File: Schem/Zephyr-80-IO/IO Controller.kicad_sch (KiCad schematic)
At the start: 37 parts, among them IC1 Z80CTC, IC2 Z80SIO, IC3 Z80SIO, J5 Conn_01x08_Pin, SW1 SW_Push, SW2 SW_Push, U1 74AHCT125, U15 PIC18F57Q84-I/PT, U2 74AHCT1G125, U4 74AHC595, U5 74AHC595, U6 74HC138

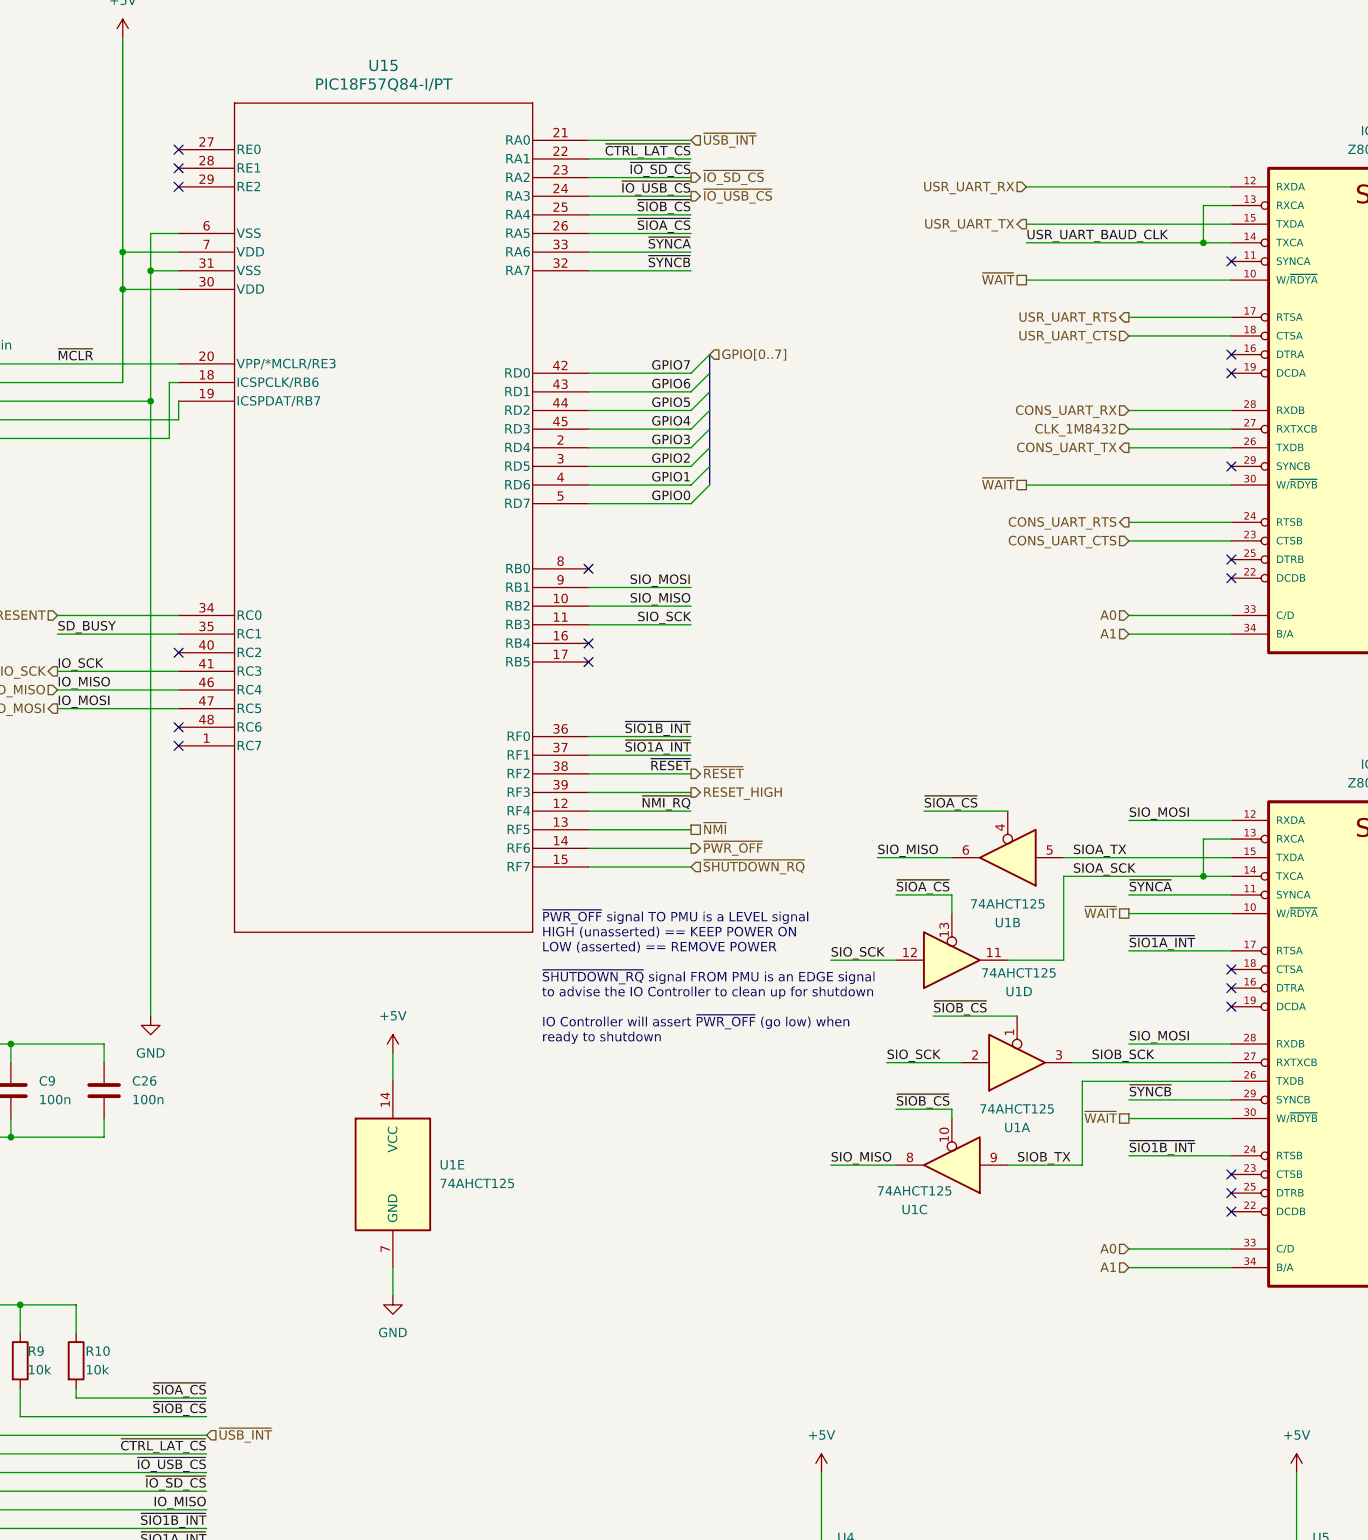
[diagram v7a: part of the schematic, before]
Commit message: Fixed a few mistakes in the IO Controller
* Wrong layer for vertical traces (should not be on the same layer as vcc plane)
* Added pull-downs for DCD for all SIOs (we don't use this line)
* Connected DCD and CTS to the MCU for SIO1 in case we want to use it to gate the SIO1
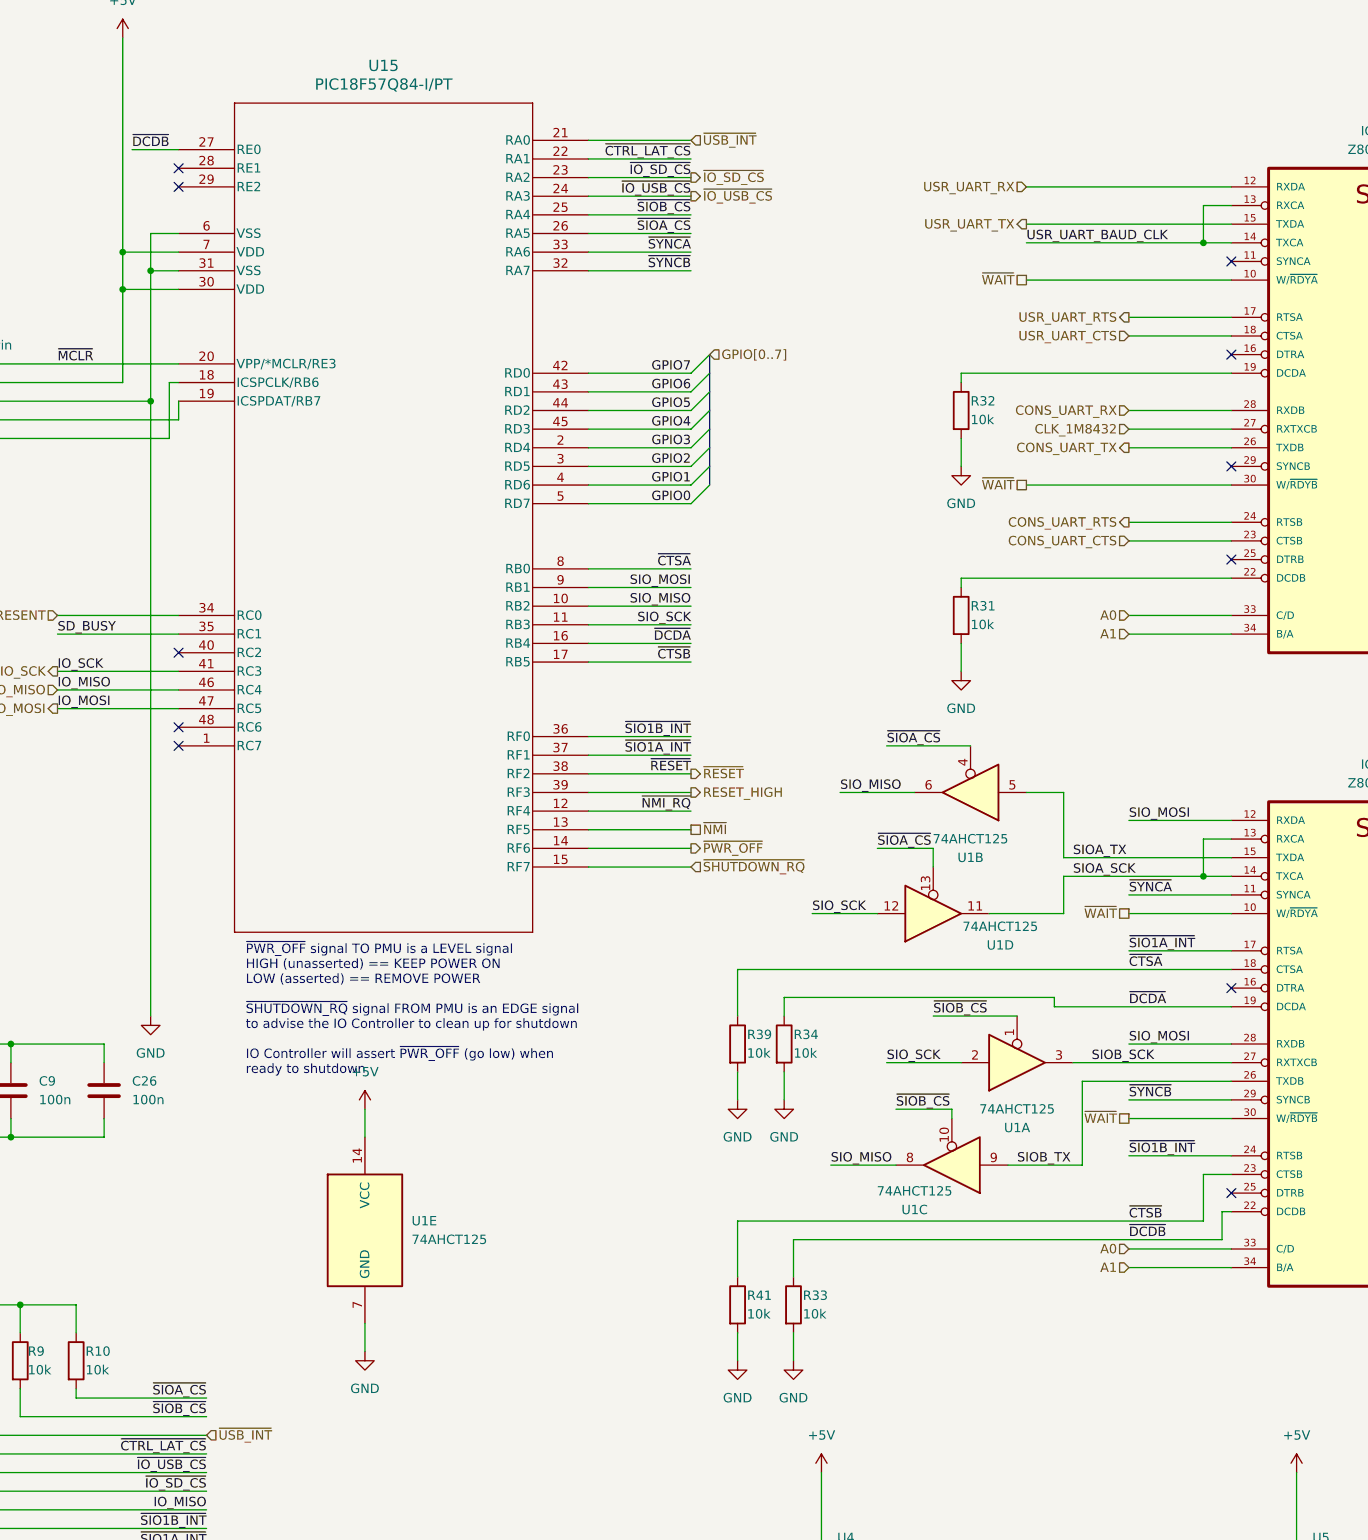
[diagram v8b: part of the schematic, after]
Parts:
- added R31, R32, R33, R34, R39, R41: 10k, Resistor_SMD:R_0603_1608Metric, symbol Device:R
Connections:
- net GND: now also R31.2, R32.2, R33.2, R34.2, R39.2, R41.2
- net ~{CTSA}: now reaches IC3.18 (CTSA)
- net ~{CTSA}: now also U15.8 (RB0), R39.1
- net ~{DCDA}: now reaches IC3.19 (DCDA)
- net ~{DCDA}: now also U15.16 (RB4), R34.1
- net ~{DCDB}: now reaches IC3.22 (DCDB)
- net ~{DCDB}: now also U15.27 (RE0), R33.1
- net ~{CTSB}: now reaches IC3.23 (CTSB)
- net ~{CTSB}: now also U15.17 (RB5), R41.1
- net at IC2.19 (DCDA): now also R32.1
- net at IC2.22 (DCDB): now also R31.1
- no-connect marks 31 -> 21
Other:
- moved on the sheet: U1B, U1D, U1E
